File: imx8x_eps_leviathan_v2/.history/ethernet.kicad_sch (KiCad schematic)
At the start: 76 parts, among them Q1 IRLML6401, Q2 BSS138, U25 DP83867CRRGZR, U26 MCP1824T-ADJE/OT, U27 TLV71310PDQNR, U28 74LVC2G07GW, Y3 25MHz

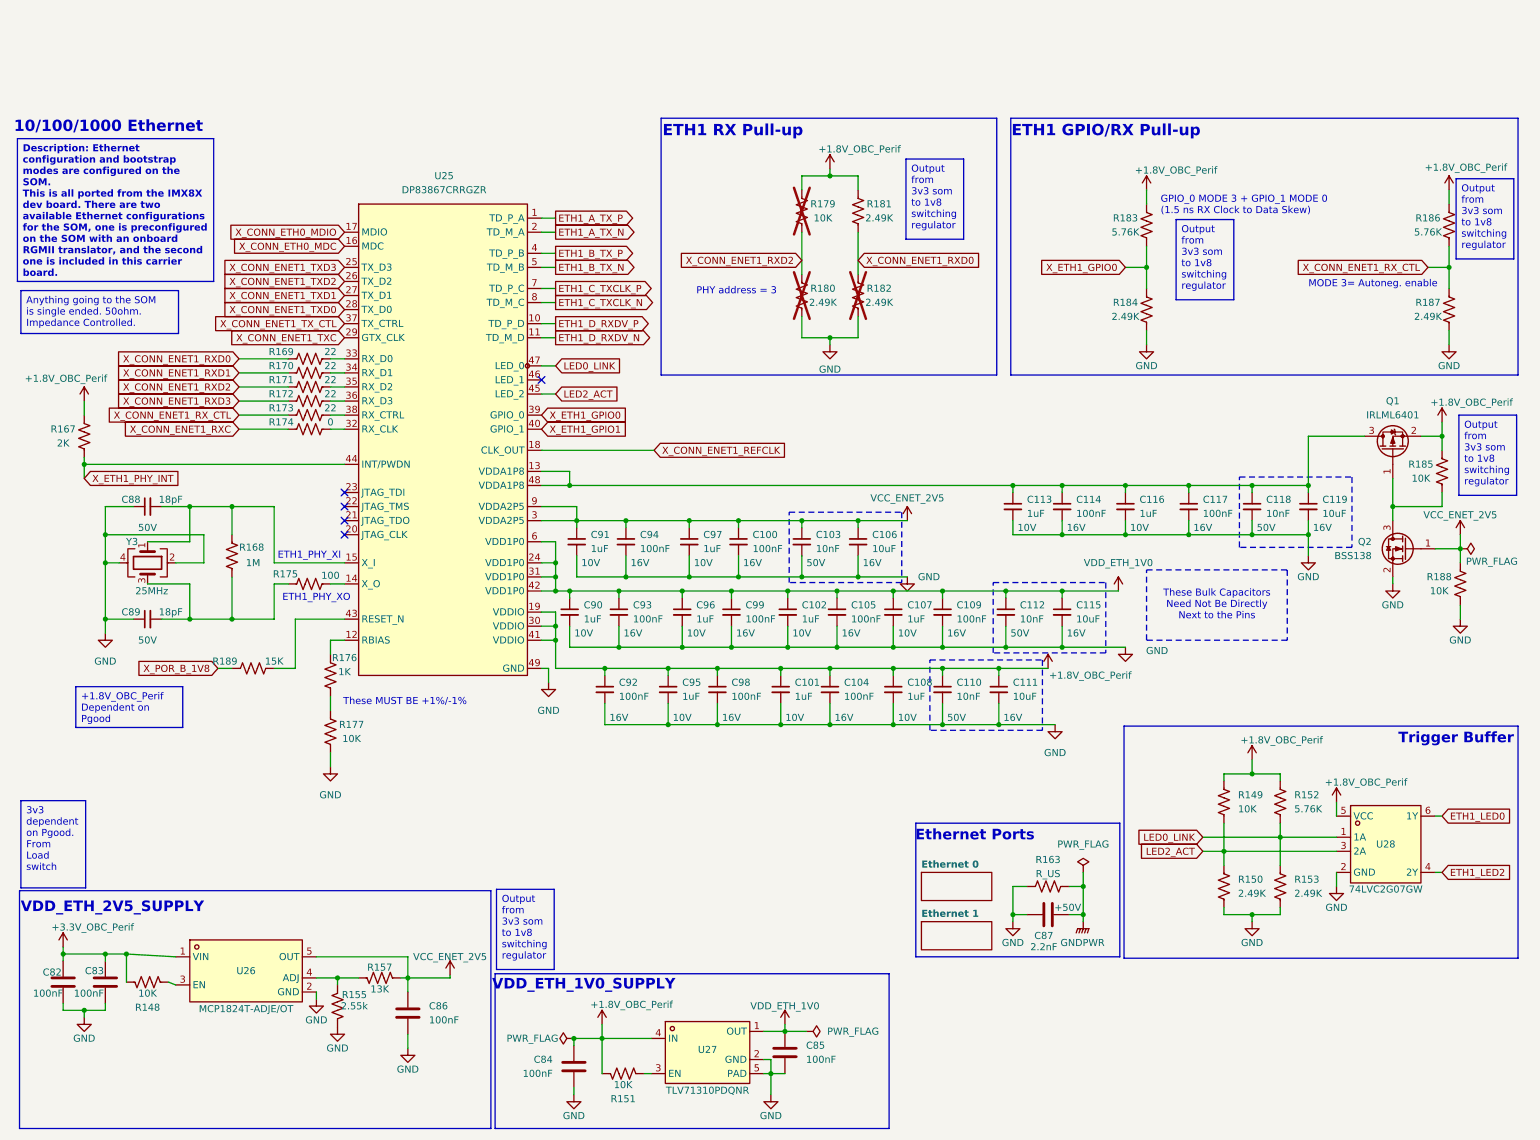
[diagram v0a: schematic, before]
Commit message: Goodies
Updated USB to USB C. Added Diodes for USB. Improved Layout. Ready for some routing.
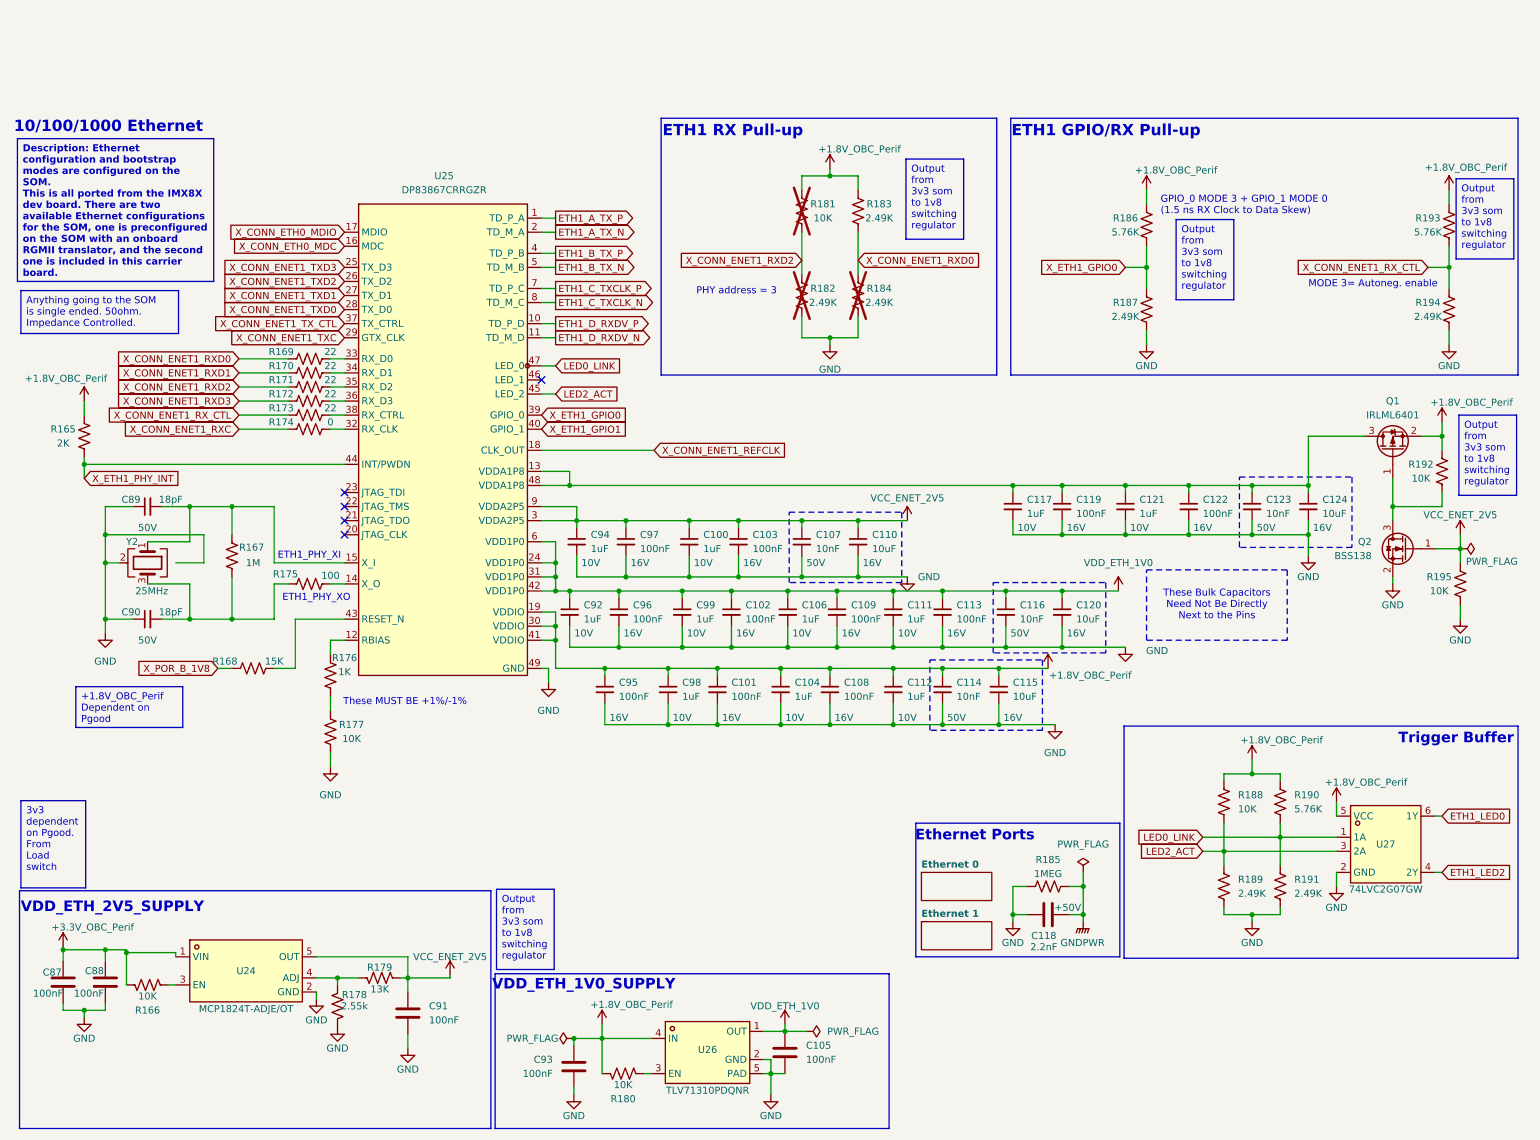
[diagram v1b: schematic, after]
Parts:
- Q1, Q2: footprint imx8_carrier_board_footprints:SOT-23 -> Package_TO_SOT_SMD:SOT-23
- R185: renamed from R163; value R_US -> 1MEG
- renumbered C97 to C100, C98 to C101, C99 to C102, C100 to C103, C101 to C104, C85 to C105, C102 to C106, C103 to C107, C104 to C108, C105 to C109, C106 to C110, C107 to C111, C108 to C112, C109 to C113, C110 to C114, C111 to C115, C112 to C116, C113 to C117, C87 to C118, C114 to C119, C115 to C120, C116 to C121, C117 to C122, C118 to C123, C119 to C124, C82 to C87, C83 to C88, C88 to C89, C89 to C90, C86 to C91, C90 to C92, C84 to C93, C91 to C94, C92 to C95, C93 to C96, C94 to C97, C95 to C98, C96 to C99, R167 to R165, R148 to R166, R168 to R167, R189 to R168, R155 to R178, R157 to R179, R151 to R180, R179 to R181, R180 to R182, R181 to R183, R182 to R184, R183 to R186, R184 to R187, R149 to R188, R150 to R189, R152 to R190, R153 to R191, R185 to R192, R186 to R193, R187 to R194, R188 to R195, U26 to U24, U27 to U26, U28 to U27, Y3 to Y2
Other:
- title: Leviathan V1 -> Leviathan V2
- moved on the sheet: R166

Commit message: Finished Layout. Board is complete
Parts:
- Y2: symbol Device:Crystal_GND24 -> imx8_carrier_board_symbol_library:Crystal_GND24
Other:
- note added: "Page 44 DPS Datasheet"

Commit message: Fixed Duplicates. Updated Gerber and BOM
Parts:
- C100, C104, C106, C111, C112, C117, C121, C92, C94, C98, C99: value 1uF -> 1u
- C101, C102, C103, C105, C108, C109, C113, C119, C122, C87, C88, C91, C93, C95, C96, C97: value 100nF -> 100n
- C107, C114, C116, C123: value 10nF -> 10n
- C110, C115, C120, C124: value 10uF -> 10u
- C118: value 2.2nF -> 2.2n
- C89, C90: value 18pF -> 18p
- R165: value 2K -> 2k
- R166, R177, R180, R181, R188, R192, R195: value 10K -> 10k
- R168: value 15K -> 15k
- R176: value 1K -> 1k
- R179: value 13K -> 13k
- R182, R183, R184, R187, R189, R191, R194: value 2.49K -> 2.49k
- R186, R190, R193: value 5.76K -> 5.76k
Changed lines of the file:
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@@
 			)
 		)
-		(property "Value" "10nF"
+		(property "Value" "10n"
 			(at 194.31 104.1463 0)
 			(show_name no)
@@
 			)
 		)
-		(property "Value" "10uF"
+		(property "Value" "10u"
 			(at 204.47 104.1463 0)
 			(show_name no)
@@
 			)
 		)
-		(property "Value" "1uF"
+		(property "Value" "1u"
 			(at 133.35 118.1163 0)
 			(show_name no)
@@
 			)
 		)
-		(property "Value" "100nF"
+		(property "Value" "100n"
 			(at 109.982 186.1819 0)
 			(show_name no)
@@
 			)
 		)
-		(property "Value" "100nF"
+		(property "Value" "100n"
 			(at 125.73 91.4463 0)
 			(show_name no)
@@
 			)
 		)
-		(property "Value" "10K"
+		(property "Value" "10k"
 			(at 36.83 172.212 90)
 			(show_name no)
@@
 			)
 		)
-		(property "Value" "5.76K"
+		(property "Value" "5.76k"
 			(at 213.36 34.29 0)
 			(show_name no)
@@
 			)
 		)
-		(property "Value" "100nF"
+		(property "Value" "100n"
 			(at 144.78 104.1463 0)
 			(show_name no)
@@
 			)
 		)
-		(property "Value" "10uF"
+		(property "Value" "10u"
 			(at 193.04 118.1163 0)
 			(show_name no)
@@
 			)
 		)
-		(property "Value" "1uF"
+		(property "Value" "1u"
 			(at 195.58 85.0963 0)
 			(show_name no)
@@
 			)
 		)
-		(property "Value" "100nF"
+		(property "Value" "100n"
 			(at 21.59 171.704 0)
 			(show_name no)
@@
 			)
 		)
-		(property "Value" "10K"
+		(property "Value" "10k"
 			(at 73.66 125.73 0)
 			(show_name no)
@@
 			)
 		)
-		(property "Value" "100nF"
+		(property "Value" "100n"
 			(at 87.63 176.5299 0)
 			(show_name no)
@@
 			)
 		)
-		(property "Value" "100nF"
+		(property "Value" "100n"
 			(at 227.33 85.0963 0)
 			(show_name no)
@@
 			)
 		)
-		(property "Value" "100nF"
+		(property "Value" "100n"
 			(at 163.83 104.1463 0)
 			(show_name no)
@@
 			)
 		)
-		(property "Value" "1uF"
+		(property "Value" "1u"
 			(at 215.9 85.0963 0)
 			(show_name no)
@@
 			)
 		)
-		(property "Value" "100nF"
+		(property "Value" "100n"
 			(at 146.05 91.4463 0)
 			(show_name no)
@@
 			)
 		)
-		(property "Value" "100nF"
+		(property "Value" "100n"
 			(at 124.46 104.1463 0)
 			(show_name no)
@@
 			)
 		)
-		(property "Value" "2.49K"
+		(property "Value" "2.49k"
 			(at 267.97 49.53 0)
 			(show_name no)
@@
 			)
 		)
-		(property "Value" "10K"
+		(property "Value" "10k"
 			(at 122.682 188.214 90)
 			(show_name no)
@@
 			)
 		)
-		(property "Value" "1K"
+		(property "Value" "1k"
 			(at 72.39 113.665 0)
 			(show_name no)
@@
 			)
 		)
-		(property "Value" "100nF"
+		(property "Value" "100n"
 			(at 121.92 118.1163 0)
 			(show_name no)
@@
 			)
 		)
-		(property "Value" "10K"
+		(property "Value" "10k"
 			(at 158.75 31.75 0)
 			(show_name no)
@@
 			)
 		)
-		(property "Value" "13K"
+		(property "Value" "13k"
 			(at 78.74 170.942 90)
 			(show_name no)
@@
 			)
 		)
-		(property "Value" "100nF"
+		(property "Value" "100n"
 			(at 204.47 85.0963 0)
 			(show_name no)
@@
 			)
 		)
-		(property "Value" "5.76K"
+		(property "Value" "5.76k"
 			(at 243.84 138.4299 0)
 			(show_name no)
@@
 			)
 		)
-		(property "Value" "1uF"
+		(property "Value" "1u"
 			(at 153.67 118.1163 0)
 			(show_name no)
@@
 			)
 		)
-		(property "Value" "100nF"
+		(property "Value" "100n"
 			(at 28.956 171.704 0)
 			(show_name no)
@@
 			)
 		)
-		(property "Value" "1uF"
+		(property "Value" "1u"
 			(at 135.89 104.1463 0)
 			(show_name no)
@@
 			)
 		)
-		(property "Value" "10nF"
+		(property "Value" "10n"
 			(at 182.88 118.1163 0)
 			(show_name no)
@@
 			)
 		)
-		(property "Value" "1uF"
+		(property "Value" "1u"
 			(at 137.16 91.4463 0)
 			(show_name no)
@@
 			)
 		)
-		(property "Value" "5.76K"
+		(property "Value" "5.76k"
 			(at 267.97 34.29 0)
 			(show_name no)
@@
 			)
 		)
-		(property "Value" "2.49K"
+		(property "Value" "2.49k"
 			(at 168.91 31.75 0)
 			(show_name no)
@@
 			)
 		)
-		(property "Value" "10nF"
+		(property "Value" "10n"
 			(at 157.48 91.4463 0)
 			(show_name no)
@@
 			)
 		)
-		(property "Value" "1uF"
+		(property "Value" "1u"
 			(at 173.99 104.1463 0)
 			(show_name no)
@@
 			)
 		)
-		(property "Value" "1uF"
+		(property "Value" "1u"
 			(at 116.84 91.44 0)
 			(show_name no)
@@
 			)
 		)
-		(property "Value" "2.49K"
+		(property "Value" "2.49k"
 			(at 168.91 46.99 0)
 			(show_name no)
@@
 			)
 		)
-		(property "Value" "18pF"
+		(property "Value" "18p"
 			(at 43.18 82.55 90)
 			(show_name no)
@@
 			)
 		)
-		(property "Value" "1uF"
+		(property "Value" "1u"
 			(at 173.99 118.1163 0)
 			(show_name no)
@@
 			)
 		)
-		(property "Value" "10uF"
+		(property "Value" "10u"
 			(at 248.92 85.0963 0)
 			(show_name no)
@@
 			)
 		)
-		(property "Value" "1uF"
+		(property "Value" "1u"
 			(at 154.94 104.1463 0)
 			(show_name no)
@@
 			)
 		)
-		(property "Value" "10K"
+		(property "Value" "10k"
 			(at 233.68 138.4299 0)
 			(show_name no)
@@
 			)
 		)
-		(property "Value" "2.49K"
+		(property "Value" "2.49k"
 			(at 213.36 49.53 0)
 			(show_name no)
@@
 			)
 		)
-		(property "Value" "100nF"
+		(property "Value" "100n"
 			(at 142.24 118.1163 0)
 			(show_name no)
@@
 			)
 		)
-		(property "Value" "2.49K"
+		(property "Value" "2.49k"
 			(at 233.68 153.6699 0)
 			(show_name no)
@@
 			)
 		)
-		(property "Value" "2K"
+		(property "Value" "2k"
 			(at 21.59 72.39 0)
 			(show_name no)
@@
 			)
 		)
-		(property "Value" "100nF"
+		(property "Value" "100n"
 			(at 155.702 183.6419 0)
 			(show_name no)
@@
 			)
 		)
-		(property "Value" "10nF"
+		(property "Value" "10n"
 			(at 238.76 85.0963 0)
 			(show_name no)
@@
 			)
 		)
-		(property "Value" "10K"
+		(property "Value" "10k"
 			(at 270.002 99.06 0)
 			(show_name no)
@@
 			)
 		)
-		(property "Value" "100nF"
+		(property "Value" "100n"
 			(at 162.56 118.1163 0)
 			(show_name no)
@@
 			)
 		)
-		(property "Value" "100nF"
+		(property "Value" "100n"
 			(at 182.88 104.1463 0)
 			(show_name no)
@@
 			)
 		)
-		(property "Value" "10K"
+		(property "Value" "10k"
 			(at 266.7 78.74 0)
 			(show_name no)
@@
 			)
 		)
-		(property "Value" "2.49K"
+		(property "Value" "2.49k"
 			(at 243.84 153.6699 0)
 			(show_name no)
@@
 			)
 		)
-		(property "Value" "1uF"
+		(property "Value" "1u"
 			(at 115.57 104.1463 0)
 			(show_name no)
@@
 			)
 		)
-		(property "Value" "15K"
+		(property "Value" "15k"
 			(at 59.69 111.76 90)
 			(show_name no)
@@
 			)
 		)
-		(property "Value" "2.49K"
+		(property "Value" "2.49k"
 			(at 158.75 46.99 0)
 			(show_name no)
@@
 			)
 		)
-		(property "Value" "2.2nF"
+		(property "Value" "2.2n"
 			(at 198.628 163.322 90)
 			(show_name no)
@@
 			)
 		)
-		(property "Value" "10uF"
+		(property "Value" "10u"
 			(at 167.64 91.4463 0)
 			(show_name no)
@@
 			)
 		)
-		(property "Value" "18pF"
+		(property "Value" "18p"
 			(at 43.18 102.87 90)
 			(show_name no)

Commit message: Fixed errors I forgot about
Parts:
- R185: value 1MEG -> 1M; footprint (none) -> EPS:R0402
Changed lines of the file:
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@@
 			)
 		)
-		(property "Value" "1MEG"
+		(property "Value" "1M"
 			(at 199.39 150.114 90)
 			(show_name no)
@@
 			)
 		)
-		(property "Footprint" ""
+		(property "Footprint" "EPS:R0402"
 			(at 199.644 151.384 90)
 			(hide yes)
